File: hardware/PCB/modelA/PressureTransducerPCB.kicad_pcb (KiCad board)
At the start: 2 copper layers, 165.1 x 25.4 mm, 24 parts, among them J1 Conn_01x05_Male, J2 MS5803_HDR, J3 JST_PowerPlug, J4 Micro_SD, U1 ATmega328PB-AU, U2 DS3231SN, U3 TPS7A0333PDBVR

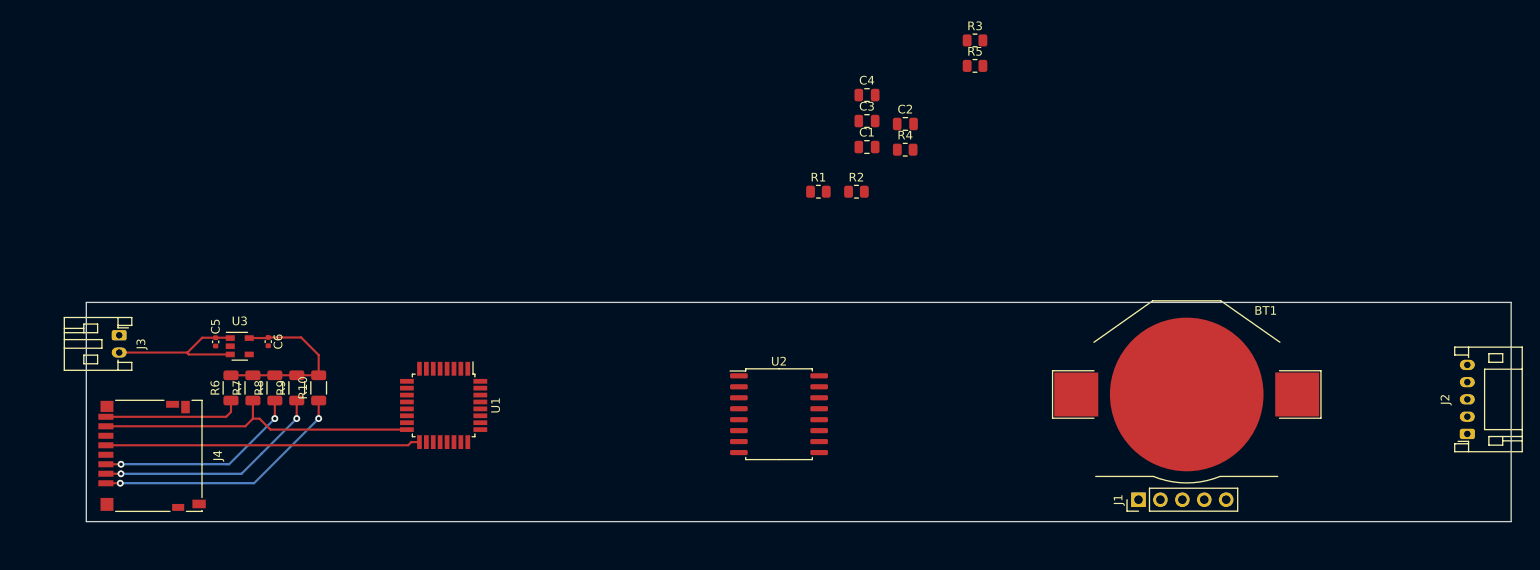
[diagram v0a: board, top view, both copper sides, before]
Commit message: Finish first layout design with minor schematic changes
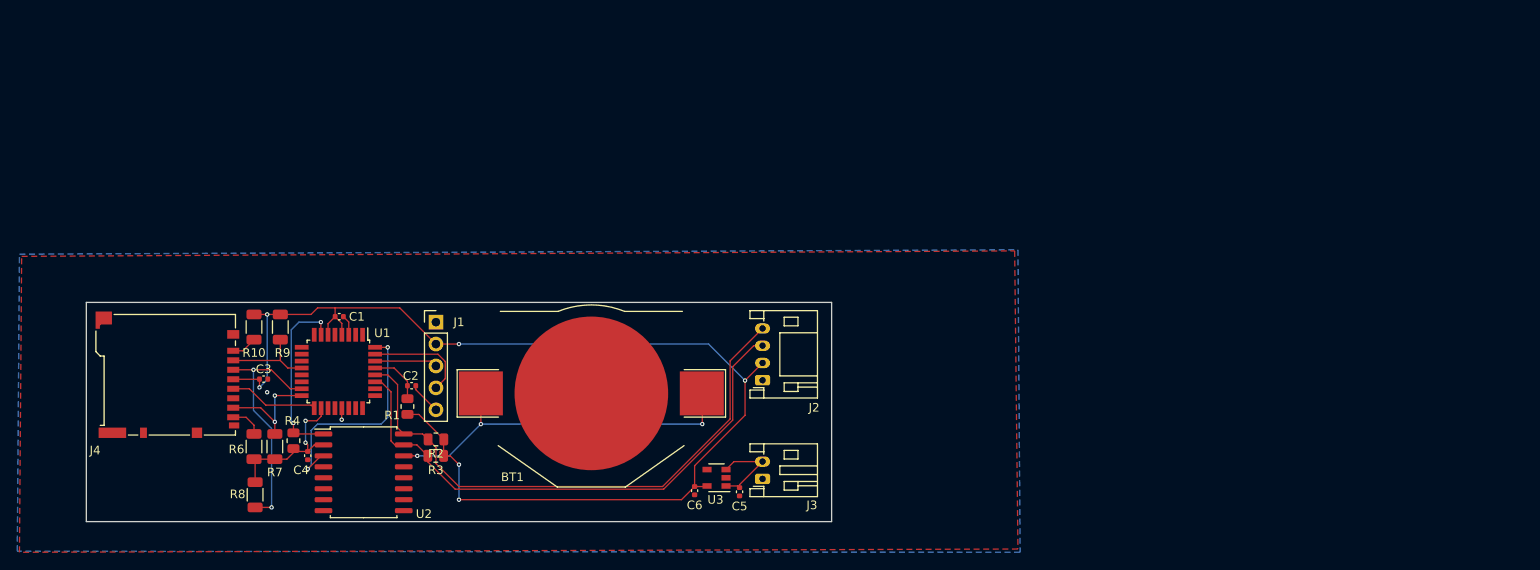
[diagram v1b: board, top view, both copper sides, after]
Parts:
- removed R5: 10K, Resistor_SMD:R_0805_2012Metric
- C1, C2, C3, C4: footprint Capacitor_SMD:C_0805_2012Metric -> Capacitor_SMD:C_0402_1005Metric
- J2: footprint Connector_JST:JST_PH_S5B-PH-K_1x05_P2.00mm_Horizontal -> Connector_JST:JST_PH_S4B-PH-K_1x04_P2.00mm_Horizontal
- J4: footprint Connector_Card:microSD_HC_Hirose_DM3D-SF -> Connector_Card:microSD_HC_Hirose_DM3BT-DSF-PEJS
- moved J1 84.0 mm to (116.7, 78.5), turned to 0 degrees
- moved J2 81.9 mm to (154.6, 85.2)
- moved R3 78.9 mm to (116.7, 94.0), turned to 180 degrees
- moved R4 78.5 mm to (100.2, 92.2), turned to 270 degrees
- moved C4 77.1 mm to (101.9, 94.0), turned to 270 degrees
- moved J3 76.4 mm to (154.6, 96.6), turned to 90 degrees
- moved C3 76.0 mm to (96.7, 85.1)
- moved BT1 69.0 mm to (134.7, 86.7), turned to 0 degrees
- moved C2 64.8 mm to (113.9, 85.9), turned to 180 degrees
- moved C1 64.2 mm to (105.5, 77.9), turned to 180 degrees
- moved C5 63.1 mm to (151.9, 98.1)
- moved U3 57.3 mm to (149.2, 96.5), turned to 180 degrees
- moved R2 56.5 mm to (116.7, 92.1), turned to 180 degrees
- moved R1 53.7 mm to (113.4, 88.3), turned to 90 degrees
- moved C6 52.3 mm to (146.7, 98.0)
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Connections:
- net +3V3 renamed +3V8
- net DTR renamed ~RESET
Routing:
- net VCC: track 21.4 -> 159.0 mm, vias 0 -> 8
- net SCL: track 0.00 -> 65.8 mm
- net SDA: track 0.00 -> 64.3 mm
- net Net-(BT1-Pad1): track 0.00 -> 43.3 mm, vias 0 -> 3
- net Net-(J4-Pad1): track 29.9 -> 2.94 mm, vias 2 -> 0
- net SCK: track 36.5 -> 10.3 mm
- net ~INT: track 0.00 -> 26.2 mm, vias 0 -> 2
- net MISO: track 37.9 -> 13.1 mm, vias 0 -> 2
- net 32KHz: track 0.00 -> 21.1 mm, vias 0 -> 2
- net CS: track 26.9 -> 10.7 mm, vias 2 -> 0
- net Net-(J4-Pad8): track 16.1 -> 3.80 mm
- net MCU_TX: track 0.00 -> 12.0 mm
- net +3V8: track 18.7 -> 10.4 mm
- net MCU_RX: track 0.00 -> 7.29 mm
- net ~RESET: track 0.00 -> 6.40 mm
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- added copper zone on B.Cu, net GND
- added copper zone on F.Cu, net GND
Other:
- board size 165.1 x 25.4 mm -> 86.4 x 25.4 mm
- net class Default: clearance 0.2 -> 0.1524; trace_width 0.25 -> 0.1524; via_dia 0.8 -> 0.508; via_drill 0.4 -> 0.254
- rule pad_to_mask_clearance: 0 -> 0.0508
- rule trace_clearance: 0.2 -> 0.1524
- rule trace_min: 0.2 -> 0.1524
- rule via_min_drill: 0.3 -> 0.254
- rule via_min_size: 0.4 -> 0.508
